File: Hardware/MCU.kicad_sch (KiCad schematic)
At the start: 38 parts, among them SW301 RESET, U301 STM32F722ZETx, Y301 24MHz

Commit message: Finalize silkscreen
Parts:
- renumbered TP305 to TP303, TP306 to TP304, TP307 to TP305, TP308 to TP306, TP309 to TP307, TP310 to TP308, TP311 to TP309, TP312 to TP310
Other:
- title: (none) -> Avionus_Flight_Controller
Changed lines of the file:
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@@
 (kicad_sch (version 20230121) (generator eeschema)
   (paper "A3")
+  (title_block
+    (title "Avionus_Flight_Controller")
+    (date "2023-11-25")
+    (rev "1.0")
+  )
   (junction (at 294.64 78.74) (diameter 0) (color 0 0 0 0)
   )
@@
   (symbol (lib_id "Connector:TestPoint") (at 182.88 142.24 270) (unit 1)
     (in_bom yes) (on_board yes) (dnp no) (fields_autoplaced)
-    (property "Reference" "TP310" (at 187.96 142.24 90)
+    (property "Reference" "TP308" (at 187.96 142.24 90)
       (effects (font (size 1.27 1.27)) (justify left))
     )
@@
       (project "Avionus_Flight_Controller"
         (path "/ddc7e940-0588-4587-8902-8ced9e615ace/fb82246b-9ed4-401c-b8a1-7e9ae6260bc5"
-          (reference "TP310") (unit 1)
+          (reference "TP308") (unit 1)
         )
       )
@@
   (symbol (lib_id "Connector:TestPoint") (at 182.88 124.46 270) (unit 1)
     (in_bom yes) (on_board yes) (dnp no) (fields_autoplaced)
-    (property "Reference" "TP306" (at 187.96 124.46 90)
+    (property "Reference" "TP304" (at 187.96 124.46 90)
       (effects (font (size 1.27 1.27)) (justify left))
     )
@@
       (project "Avionus_Flight_Controller"
         (path "/ddc7e940-0588-4587-8902-8ced9e615ace/fb82246b-9ed4-401c-b8a1-7e9ae6260bc5"
-          (reference "TP306") (unit 1)
+          (reference "TP304") (unit 1)
         )
       )
@@
   (symbol (lib_id "Connector:TestPoint") (at 182.88 139.7 270) (unit 1)
     (in_bom yes) (on_board yes) (dnp no) (fields_autoplaced)
-    (property "Reference" "TP309" (at 187.96 139.7 90)
+    (property "Reference" "TP307" (at 187.96 139.7 90)
       (effects (font (size 1.27 1.27)) (justify left))
     )
@@
       (project "Avionus_Flight_Controller"
         (path "/ddc7e940-0588-4587-8902-8ced9e615ace/fb82246b-9ed4-401c-b8a1-7e9ae6260bc5"
-          (reference "TP309") (unit 1)
+          (reference "TP307") (unit 1)
         )
       )
@@
   (symbol (lib_id "Connector:TestPoint") (at 182.88 220.98 270) (unit 1)
     (in_bom yes) (on_board yes) (dnp no) (fields_autoplaced)
-    (property "Reference" "TP312" (at 187.96 220.98 90)
+    (property "Reference" "TP310" (at 187.96 220.98 90)
       (effects (font (size 1.27 1.27)) (justify left))
     )
@@
       (project "Avionus_Flight_Controller"
         (path "/ddc7e940-0588-4587-8902-8ced9e615ace/fb82246b-9ed4-401c-b8a1-7e9ae6260bc5"
-          (reference "TP312") (unit 1)
+          (reference "TP310") (unit 1)
         )
       )
@@
   (symbol (lib_id "Connector:TestPoint") (at 182.88 132.08 270) (unit 1)
     (in_bom yes) (on_board yes) (dnp no) (fields_autoplaced)
-    (property "Reference" "TP307" (at 187.96 132.08 90)
+    (property "Reference" "TP305" (at 187.96 132.08 90)
       (effects (font (size 1.27 1.27)) (justify left))
     )
@@
       (project "Avionus_Flight_Controller"
         (path "/ddc7e940-0588-4587-8902-8ced9e615ace/fb82246b-9ed4-401c-b8a1-7e9ae6260bc5"
-          (reference "TP307") (unit 1)
+          (reference "TP305") (unit 1)
         )
       )
@@
   (symbol (lib_id "Connector:TestPoint") (at 182.88 134.62 270) (unit 1)
     (in_bom yes) (on_board yes) (dnp no) (fields_autoplaced)
-    (property "Reference" "TP308" (at 187.96 134.62 90)
+    (property "Reference" "TP306" (at 187.96 134.62 90)
       (effects (font (size 1.27 1.27)) (justify left))
     )
@@
       (project "Avionus_Flight_Controller"
         (path "/ddc7e940-0588-4587-8902-8ced9e615ace/fb82246b-9ed4-401c-b8a1-7e9ae6260bc5"
-          (reference "TP308") (unit 1)
+          (reference "TP306") (unit 1)
         )
       )
@@
   (symbol (lib_id "Connector:TestPoint") (at 182.88 121.92 270) (unit 1)
     (in_bom yes) (on_board yes) (dnp no) (fields_autoplaced)
-    (property "Reference" "TP305" (at 187.96 121.92 90)
+    (property "Reference" "TP303" (at 187.96 121.92 90)
       (effects (font (size 1.27 1.27)) (justify left))
     )
@@
       (project "Avionus_Flight_Controller"
         (path "/ddc7e940-0588-4587-8902-8ced9e615ace/fb82246b-9ed4-401c-b8a1-7e9ae6260bc5"
-          (reference "TP305") (unit 1)
+          (reference "TP303") (unit 1)
         )
       )
@@
   (symbol (lib_id "Connector:TestPoint") (at 182.88 210.82 270) (unit 1)
     (in_bom yes) (on_board yes) (dnp no) (fields_autoplaced)
-    (property "Reference" "TP311" (at 187.96 210.82 90)
+    (property "Reference" "TP309" (at 187.96 210.82 90)
       (effects (font (size 1.27 1.27)) (justify left))
     )
@@
       (project "Avionus_Flight_Controller"
         (path "/ddc7e940-0588-4587-8902-8ced9e615ace/fb82246b-9ed4-401c-b8a1-7e9ae6260bc5"
-          (reference "TP311") (unit 1)
-        )
-      )
+          (reference "TP309") (unit 1)
+        )
+      )

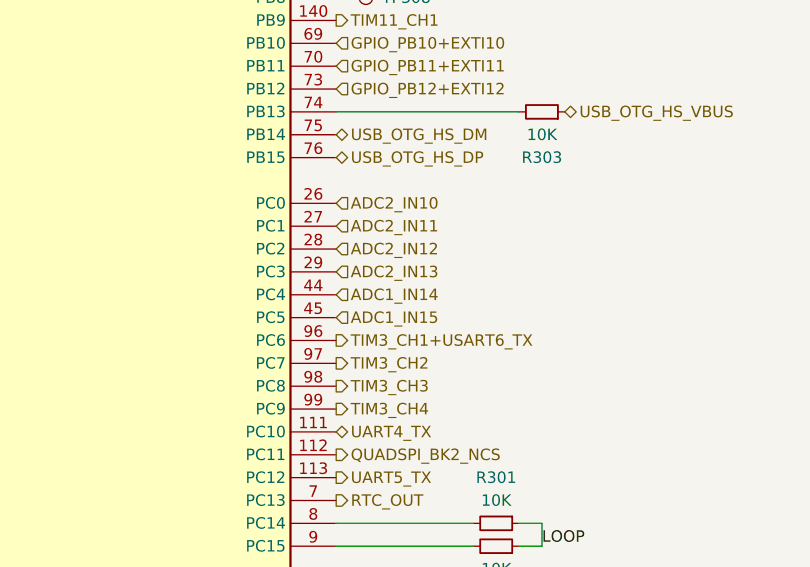
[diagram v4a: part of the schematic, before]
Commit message: Swap ADC connections for simultaneous power measurement
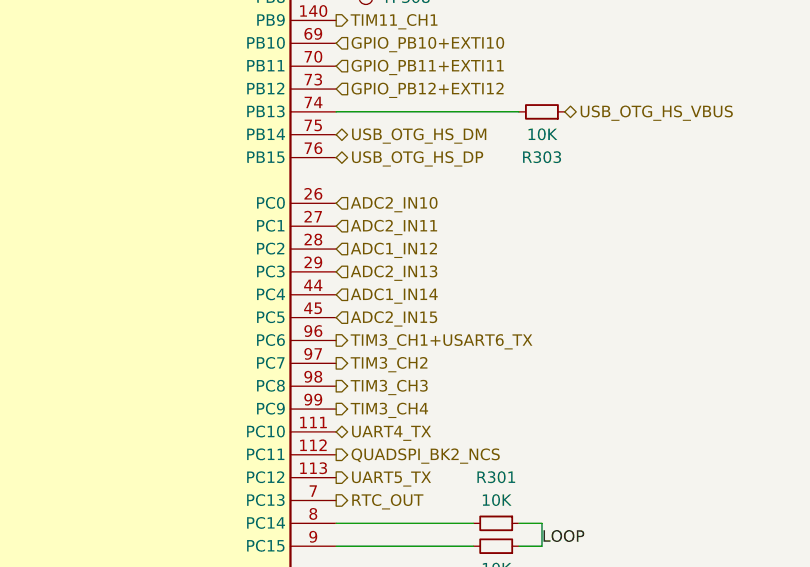
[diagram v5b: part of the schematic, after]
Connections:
- net ADC1_IN15 renamed ADC2_IN15
- net ADC2_IN12 renamed ADC1_IN12
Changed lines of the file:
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@@
     (effects (font (size 1.27 1.27)) (justify left))
   )
-  (hierarchical_label "ADC1_IN15" (shape input) (at 182.88 177.8 0) (fields_autoplaced)
+  (hierarchical_label "ADC2_IN15" (shape input) (at 182.88 177.8 0) (fields_autoplaced)
     (effects (font (size 1.27 1.27)) (justify left))
   )
@@
     (effects (font (size 1.27 1.27)) (justify left))
   )
-  (hierarchical_label "ADC2_IN12" (shape input) (at 182.88 170.18 0) (fields_autoplaced)
+  (hierarchical_label "ADC1_IN12" (shape input) (at 182.88 170.18 0) (fields_autoplaced)
     (effects (font (size 1.27 1.27)) (justify left))
   )
